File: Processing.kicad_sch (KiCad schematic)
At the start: 6 parts, among them IC10 MT29F2G01ABAGDWB-IT_G_TR, IC11 DS90LV011AHMF_NOPB, IC12 MXL86110I-AQB-R, IC8 XMC7200D-E272K8384AA, IC9 MT29F2G01ABAGDWB-IT_G_TR, Y1 DSC1101DM2-012.0000

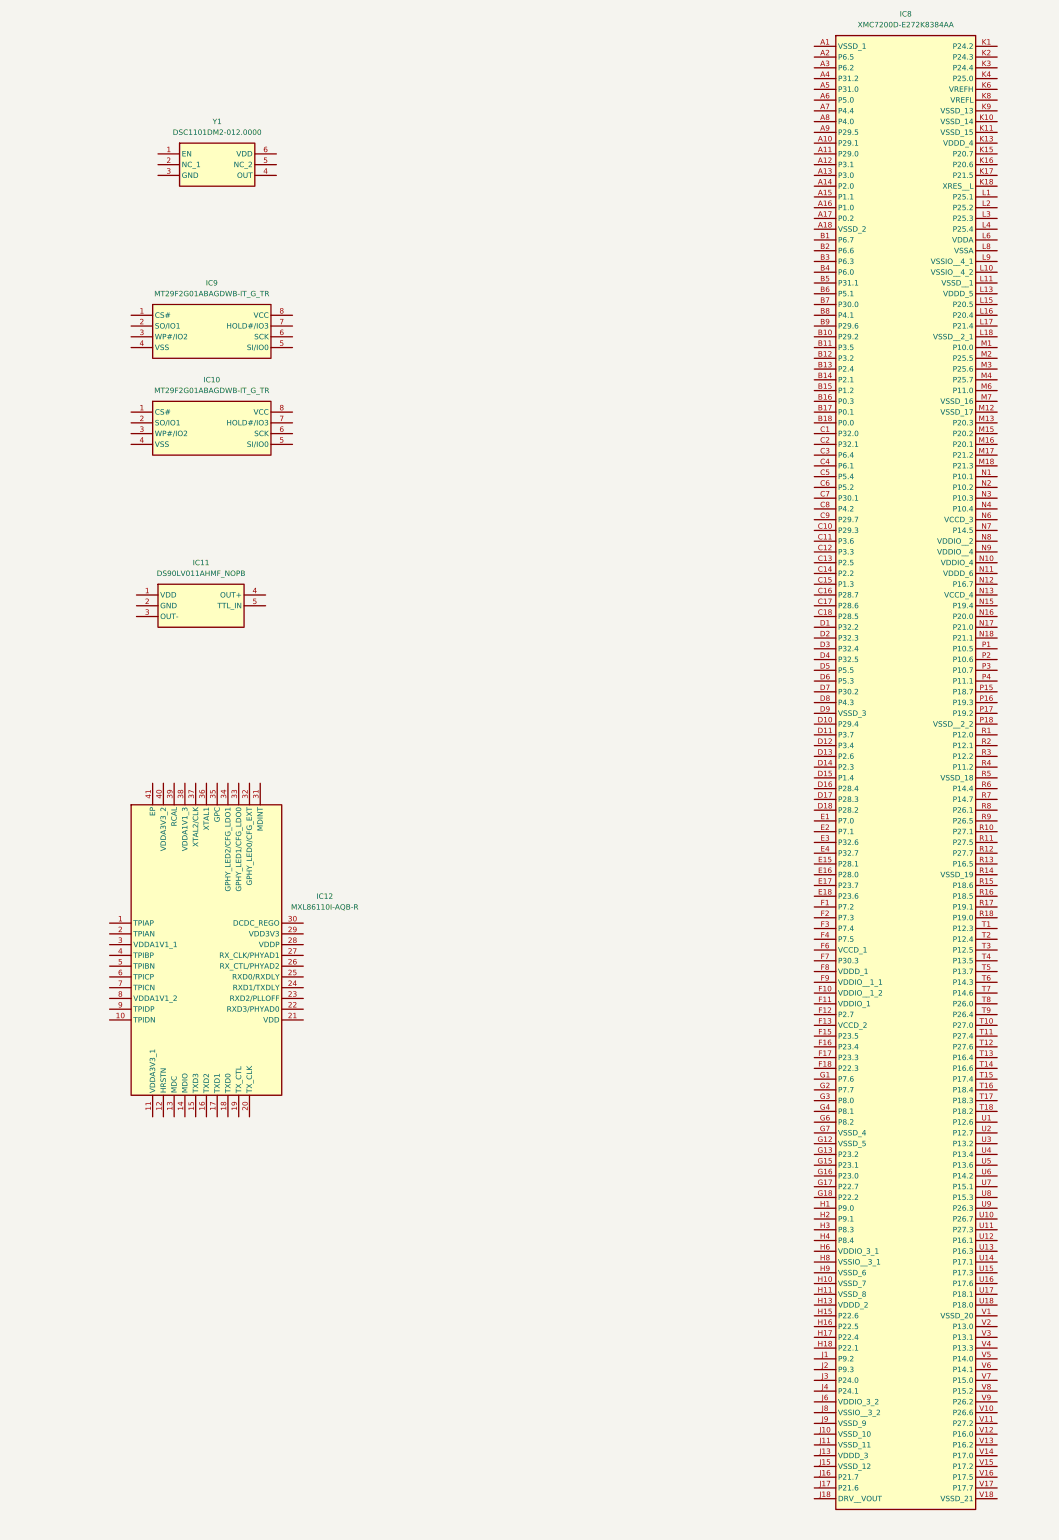
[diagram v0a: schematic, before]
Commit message: Ethernet Connections made; SPI connections made; TODO list in processing schem
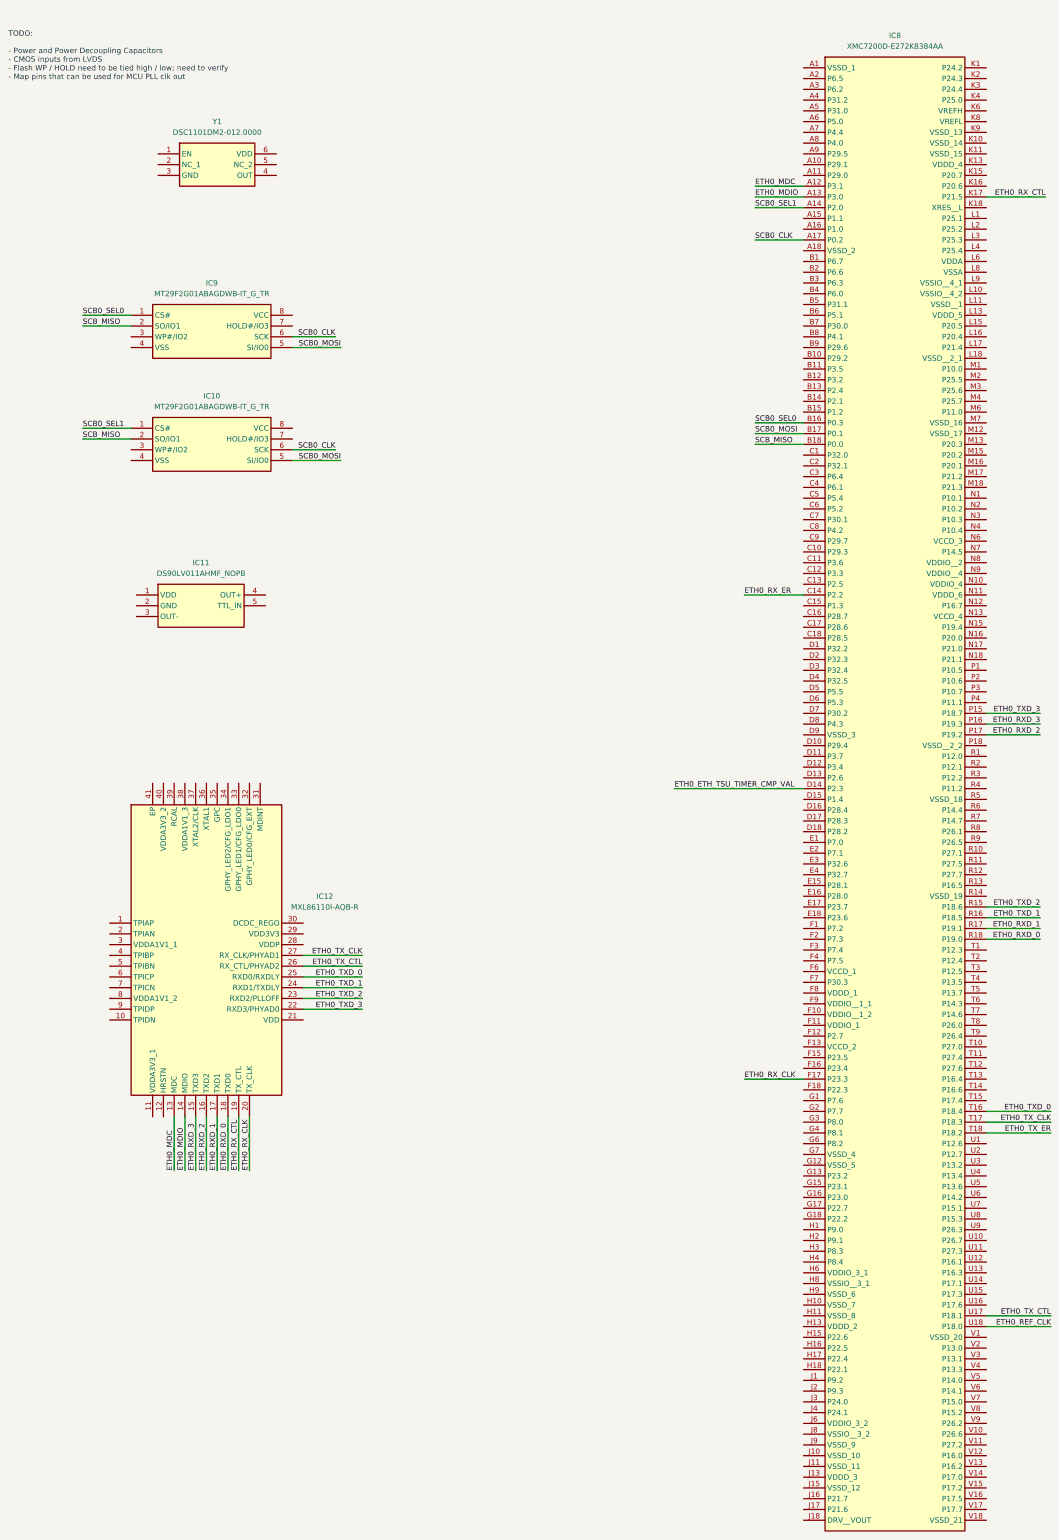
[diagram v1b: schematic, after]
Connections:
- net SCB0_SEL0: now reaches IC9.1 (CS#)
- net SCB0_SEL0: now also IC8.B16 (P0.3)
- net SCB_MISO: now reaches IC9.2 (SO/IO1)
- net SCB_MISO: now also IC10.2 (SO/IO1), IC8.B18 (P0.0)
- net SCB0_MOSI: now reaches IC9.5 (SI/IO0)
- net SCB0_MOSI: now also IC10.5 (SI/IO0), IC8.B17 (P0.1)
- net SCB0_CLK: now reaches IC9.6 (SCK)
- net SCB0_CLK: now also IC10.6 (SCK), IC8.A17 (P0.2)
- net ETH0_MDC: now reaches IC12.13 (MDC)
- net ETH0_MDC: now also IC8.A12 (P3.1)
- net ETH0_MDIO: now reaches IC12.14 (MDIO)
- net ETH0_MDIO: now also IC8.A13 (P3.0)
- net ETH0_RXD_3: now reaches IC12.15 (TXD3)
- net ETH0_RXD_3: now also IC8.P16 (P19.3)
- net ETH0_RXD_2: now reaches IC12.16 (TXD2)
- net ETH0_RXD_2: now also IC8.P17 (P19.2)
- net ETH0_RXD_1: now reaches IC12.17 (TXD1)
- net ETH0_RXD_1: now also IC8.R17 (P19.1)
- net ETH0_RXD_0: now reaches IC12.18 (TXD0)
- net ETH0_RXD_0: now also IC8.R18 (P19.0)
- net ETH0_RX_CTL: now reaches IC12.19 (TX_CTL)
- net ETH0_RX_CTL: now also IC8.K17 (P21.5)
- net ETH0_RX_CLK: now reaches IC12.20 (TX_CLK)
- net ETH0_RX_CLK: now also IC8.F17 (P23.3)
- net ETH0_TXD_3: now reaches IC12.22 (RXD3/PHYAD0)
- net ETH0_TXD_3: now also IC8.P15 (P18.7)
- net ETH0_TXD_2: now reaches IC12.23 (RXD2/PLLOFF)
- net ETH0_TXD_2: now also IC8.R15 (P18.6)
- net ETH0_TXD_1: now reaches IC12.24 (RXD1/TXDLY)
- net ETH0_TXD_1: now also IC8.R16 (P18.5)
- net ETH0_TXD_0: now reaches IC12.25 (RXD0/RXDLY)
- net ETH0_TXD_0: now also IC8.T16 (P18.4)
- net ETH0_TX_CTL: now reaches IC12.26 (RX_CTL/PHYAD2)
- net ETH0_TX_CTL: now also IC8.U17 (P18.1)
- net ETH0_TX_CLK: now reaches IC12.27 (RX_CLK/PHYAD1)
- net ETH0_TX_CLK: now also IC8.T17 (P18.3)
- net SCB0_SEL1: now reaches IC10.1 (CS#)
- net SCB0_SEL1: now also IC8.A14 (P2.0)
- net ETH0_RX_ER: now reaches IC8.C14 (P2.2)
- net ETH0_ETH_TSU_TIMER_CMP_VAL: now reaches IC8.D14 (P2.3)
- net ETH0_TX_ER: now reaches IC8.T18 (P18.2)
- net ETH0_REF_CLK: now reaches IC8.U18 (P18.0)
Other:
- note added: "TODO: - Power and Power Decoupling Capacitors - CMOS inputs from LVDS - Flash WP / HOLD need to be tied high / low; need to verify - Map pins that can be used for MCU PLL clk out"

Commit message: Processing Updates
Added LVCMOS connections to MCU, added power regulation to MCU (NOT COMPLETE!)
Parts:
- added C11, C12: 10uF, symbol Device:C
- added Q1: ZXT849K, symbol Simulation_SPICE:NPN
- added R3: 0.1, symbol Device:R
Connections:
- net VSSD: now reaches IC8.A1 (VSSD_1)
- net VSSD: now also IC8.A18 (VSSD_2), IC8.D9 (VSSD_3), IC8.G12 (VSSD_5), IC8.G7 (VSSD_4), IC8.H10 (VSSD_7), IC8.H11 (VSSD_8), IC8.H9 (VSSD_6), IC8.J10 (VSSD_10), IC8.J11 (VSSD_11), IC8.J15 (VSSD_12), IC8.J9 (VSSD_9), IC8.K10 (VSSD_14), IC8.K11 (VSSD_15), IC8.K9 (VSSD_13), IC8.L11 (VSSD__1), IC8.M12 (VSSD_17), IC8.M7 (VSSD_16), IC8.R14 (VSSD_19), IC8.R5 (VSSD_18), IC8.V1 (VSSD_20), IC8.V18 (VSSD_21)
- net D_IN1: now reaches IC8.A6 (P5.0)
- net D_IN2: now reaches IC8.A8 (P4.0)
- net ADC0_0: now reaches IC8.B4 (P6.0)
- net D_IN6: now reaches IC8.B6 (P5.1)
- net D_IN5: now reaches IC8.B8 (P4.1)
- net ADC0_1: now reaches IC8.C4 (P6.1)
- net D_IN3: now reaches IC8.C6 (P5.2)
- net D_IN4: now reaches IC8.C8 (P4.2)
- net D_IN8: now reaches IC8.D6 (P5.3)
- net D_IN7: now reaches IC8.D8 (P4.3)
- net VDDIO: now reaches IC8.F10 (VDDIO__1_2)
- net VDDIO: now also IC8.F11 (VDDIO_1), IC8.F9 (VDDIO__1_1), IC8.H6 (VDDIO_3_1), IC8.J6 (VDDIO_3_2), IC8.N10 (VDDIO_4), IC8.N8 (VDDIO__2), IC8.N9 (VDDIO__4)
- net +3V3: now reaches IC8.F8 (VDDD_1)
- net +3V3: now also IC8.H13 (VDDD_2), IC8.J13 (VDDD_3), IC8.K13 (VDDD_4), IC8.L13 (VDDD_5), IC8.N11 (VDDD_6), C11.1, Q1.1 (C)
- net VSSIO: now reaches IC8.H8 (VSSIO__3_1)
- net VSSIO: now also IC8.J8 (VSSIO__3_2), IC8.L10 (VSSIO__4_2), IC8.L9 (VSSIO__4_1)
- net VREFH: now reaches IC8.K6 (VREFH)
- net VREFL: now reaches IC8.K8 (VREFL)
- net VDDA: now reaches IC8.L6 (VDDA)
- net VSSA: now reaches IC8.L8 (VSSA)
- net D_CTR: now reaches IC8.M16 (P20.1)
- net D_CLK: now reaches IC8.M17 (P21.2)
- new net DRV_VOUT: Q1.2 (B)
- new net EXT_PS_CTL0: Q1.3 (E), R3.1
- new net EXT_PS_CTL1: C12.1, R3.2
- new net GNDPWR: C11.2, C12.2
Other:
- note added: "Core External Regulator"
- note added: "TODO: - Power and Power Decoupling Capacitors - Flash WP / HOLD need to be tied high / low; need to verify - Map pins that can be used for MCU PLL clk out"
- note removed: "TODO: - Power and Power Decoupling Capacitors - CMOS inputs from LVDS - Flash WP / HOLD need to be tied high / low; need to verify - Map pins that can be used for MCU PLL clk out"

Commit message: Added lots more connections
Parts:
- added C13, C15: 0.1uF, symbol Device:C_Polarized
- added C14: 1nF, symbol Device:C_Polarized
- added C23: 15pF, symbol Device:C
- added C24: 0.1uF, symbol Device:C
- added C25: 0.1F, symbol Device:C
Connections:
- net GNDPWR is gone; now on net GND: C11.2, C12.2
- net VDDA is gone; now on net +3V3: IC8.L6 (VDDA)
- net VDDIO is gone; now on net +3V3: IC8.F10 (VDDIO__1_2), IC8.F11 (VDDIO_1), IC8.F9 (VDDIO__1_1), IC8.H6 (VDDIO_3_1), IC8.J6 (VDDIO_3_2), IC8.N10 (VDDIO_4), IC8.N8 (VDDIO__2), IC8.N9 (VDDIO__4)
- net VREFH is gone; now on net +3V3: IC8.K6 (VREFH)
- net VREFL is gone; now on net GNDSIG_D: IC8.K8 (VREFL)
- net VSSD is gone; now on net GNDSIG_D: IC8.A1 (VSSD_1), IC8.A18 (VSSD_2), IC8.D9 (VSSD_3), IC8.G12 (VSSD_5), IC8.G7 (VSSD_4), IC8.H10 (VSSD_7), IC8.H11 (VSSD_8), IC8.H9 (VSSD_6), IC8.J10 (VSSD_10), IC8.J11 (VSSD_11), IC8.J15 (VSSD_12), IC8.J9 (VSSD_9), IC8.K10 (VSSD_14), IC8.K11 (VSSD_15), IC8.K9 (VSSD_13), IC8.L11 (VSSD__1), IC8.M12 (VSSD_17), IC8.M7 (VSSD_16), IC8.R14 (VSSD_19), IC8.R5 (VSSD_18), IC8.V1 (VSSD_20), IC8.V18 (VSSD_21)
- net VSSIO is gone; now on net GNDSIG_D: IC8.H8 (VSSIO__3_1), IC8.J8 (VSSIO__3_2), IC8.L10 (VSSIO__4_2), IC8.L9 (VSSIO__4_1)
- net +3V3: now also IC10.8 (VCC), IC11.1 (VDD), IC12.11 (VDDA3V3_1), IC12.29 (VDD3V3), IC12.40 (VDDA3V3_2), IC9.8 (VCC), Y1.6 (VDD), C13.1, C14.1, C15.1, C24.1, C25.1
- net DRV_VOUT: now also IC8.J18 (DRV__VOUT)
- net D_CLK: now also IC8.E17 (P23.7); no longer IC8.M17 (P21.2)
- net D_CTR: now also IC8.D17 (P28.3); no longer IC8.M16 (P20.1)
- net EXT_PS_CTL0: now also IC8.H18 (P22.1)
- net EXT_PS_CTL1: now also IC8.F13 (VCCD_2), IC8.F6 (VCCD_1), IC8.G18 (P22.2), IC8.N13 (VCCD_4), IC8.N6 (VCCD_3)
- net SCB0_CLK: no longer IC10.6 (SCK)
- net SCB0_MOSI: no longer IC10.5 (SI/IO0)
- net SCB0_SEL1: no longer IC10.1 (CS#)
- net GND: now reaches IC10.4 (VSS)
- net GND: now also IC11.2 (GND), IC12.41 (EP), IC9.4 (VSS), C13.2, C14.2, C15.2, C23.2, C24.2, C25.2
- net GNDSIG_D: now reaches Y1.3 (GND)
- net GNDSIG_D: now also IC8.L18 (VSSD__2_1), IC8.P18 (VSSD__2_2)
- net ECO_IN: now reaches Y1.4 (OUT)
- net ECO_IN: now also IC8.M17 (P21.2), C23.1
- net VDD1V1: now reaches IC12.21 (VDD)
- net VDD1V1: now also IC12.3 (VDDA1V1_1), IC12.30 (DCDC_REGO), IC12.38 (VDDA1V1_3), IC12.8 (VDDA1V1_2)
- net LVDS_CLK_N: now reaches IC11.3 (OUT-)
- net LVDS_CLK_P: now reaches IC11.4 (OUT+)
- net CLK_OUT: now reaches IC11.5 (TTL_IN)
- net SCB2_SEL0: now reaches IC8.T6 (P14.3)
- net SCB2_SEL0: now also IC10.1 (CS#)
- net SCB2_CLK: now reaches IC8.U6 (P14.2)
- net SCB2_CLK: now also IC10.6 (SCK)
- net SCB2_MISO: now reaches IC8.V5 (P14.0)
- net SCB2_MISO: now also IC10.2 (SO/IO1)
- net SCB2_MOSI: now reaches IC8.V6 (P14.1)
- net SCB2_MOSI: now also IC10.5 (SI/IO0)
- net SCB_MISO renamed SCB0_MISO
- net SCB0_MISO: no longer IC10.2 (SO/IO1)
- net VSSA renamed GNDSIG_A
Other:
- note added: "Ethernet"
- note added: "Grounds"
- note added: "LVDS Clock"
- note added: "Memory"
- note added: "Reference Oscillator"
- moved on the sheet: IC10, IC11, IC9, Y1
